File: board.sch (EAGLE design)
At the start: 27 parts

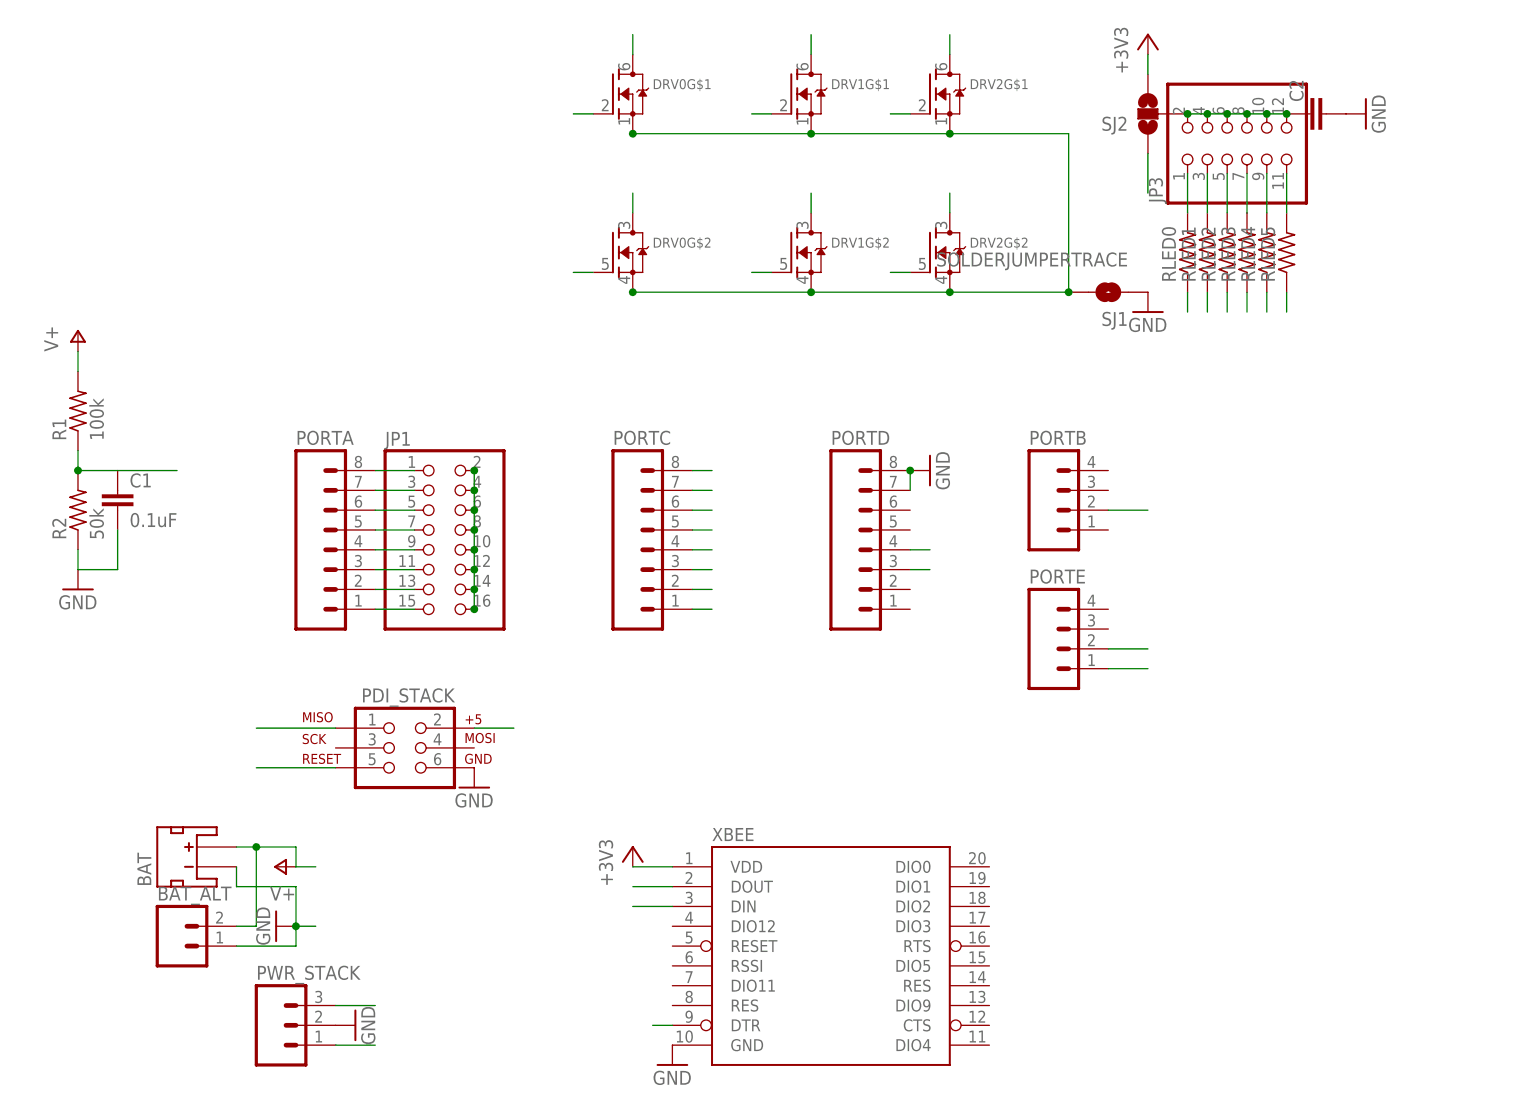
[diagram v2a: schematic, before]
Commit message: bigger cap for the leds
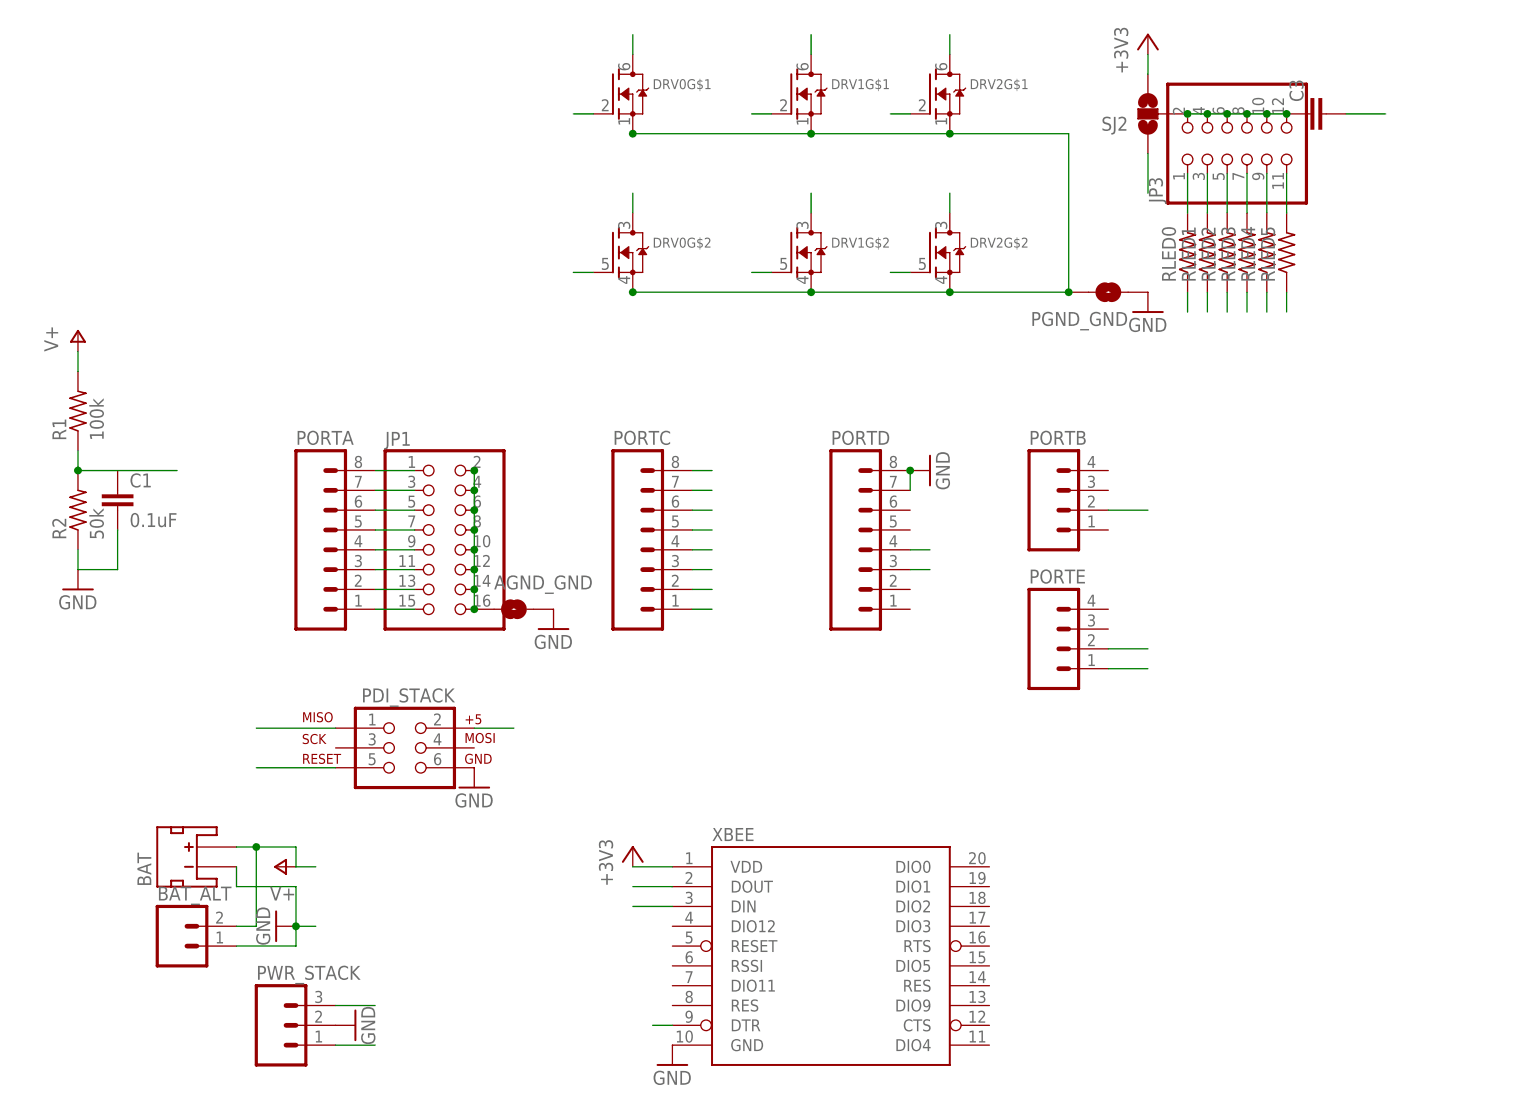
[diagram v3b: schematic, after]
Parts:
- removed C2: (no value), resistor:C-EUC0805K
- added AGND_GND: SOLDERJUMPERTRACE, SparkFun-Passives:SOLDERJUMPERTRACE
- added C3: (no value), rcl:C-EUC1210
- renumbered SJ1 to PGND_GND
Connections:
- removed net GND_PWR: DRV0G$1.S, DRV0G$2.S, DRV1G$1.S, DRV1G$2.S, DRV2G$1.S, DRV2G$2.S, PGND_GND.2
- new net PGND: C3.2, DRV0G$1.S, DRV0G$2.S, DRV1G$1.S, DRV1G$2.S, DRV2G$1.S, DRV2G$2.S, PGND_GND.2
- net AGND: now also AGND_GND.1
- net GND: now also AGND_GND.2; no longer C2.2
- net VLED: now also C3.1; no longer C2.1
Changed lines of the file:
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@@
 <part name="RLED5" library="resistor" deviceset="R-US_" device="R0805"/>
 <part name="+3V2" library="supply1" deviceset="+3V3" device=""/>
-<part name="C2" library="resistor" deviceset="C-EU" device="C0805K"/>
-<part name="GND7" library="supply1" deviceset="GND" device=""/>
-<part name="SJ1" library="SparkFun-Passives" deviceset="SOLDERJUMPER" device="TRACE"/>
+<part name="PGND_GND" library="SparkFun-Passives" deviceset="SOLDERJUMPER" device="TRACE"/>
 <part name="GND8" library="supply1" deviceset="GND" device=""/>
 <part name="JP3" library="pinhead" deviceset="PINHD-2X6" device="/90"/>
+<part name="AGND_GND" library="SparkFun-Passives" deviceset="SOLDERJUMPER" device="TRACE"/>
+<part name="GND9" library="supply1" deviceset="GND" device=""/>
+<part name="C3" library="rcl" deviceset="C-EU" device="C1210"/>
 </parts>
 <sheets>
@@
 <instance part="RLED5" gate="G$1" x="127" y="134.62" rot="R90"/>
 <instance part="+3V2" gate="G$1" x="43.18" y="58.42"/>
-<instance part="C2" gate="G$1" x="129.54" y="152.4" rot="R90"/>
-<instance part="GND7" gate="1" x="137.16" y="152.4" rot="R90"/>
-<instance part="SJ1" gate="1" x="104.14" y="129.54" rot="R180"/>
+<instance part="PGND_GND" gate="1" x="104.14" y="129.54" smashed="yes" rot="R180">
+<attribute name="NAME" x="106.68" y="127" size="1.778" layer="95" rot="R180"/>
+</instance>
 <instance part="GND8" gate="1" x="109.22" y="127"/>
 <instance part="JP3" gate="A" x="119.38" y="147.32" rot="R90"/>
+<instance part="AGND_GND" gate="1" x="27.94" y="88.9" smashed="yes">
+<attribute name="NAME" x="25.4" y="91.44" size="1.778" layer="95"/>
+</instance>
+<instance part="GND9" gate="1" x="33.02" y="86.36"/>
+<instance part="C3" gate="G$1" x="129.54" y="152.4" rot="R90"/>
 </instances>
 <busses>
@@
 </segment>
 <segment>
-<pinref part="C2" gate="G$1" pin="2"/>
-<pinref part="GND7" gate="1" pin="GND"/>
-</segment>
-<segment>
-<pinref part="SJ1" gate="1" pin="1"/>
+<pinref part="PGND_GND" gate="1" pin="1"/>
 <pinref part="GND8" gate="1" pin="GND"/>
+</segment>
+<segment>
+<pinref part="AGND_GND" gate="1" pin="2"/>
+<pinref part="GND9" gate="1" pin="GND"/>
 </segment>
 </net>
@@
 </segment>
 </net>
-<net name="GND_PWR" class="1">
+<net name="PGND" class="1">
 <segment>
 <pinref part="DRV0" gate="G$1" pin="S"/>
@@
 <junction x="43.18" y="149.86"/>
 <junction x="43.18" y="129.54"/>
-<pinref part="SJ1" gate="1" pin="2"/>
+<pinref part="PGND_GND" gate="1" pin="2"/>
 <junction x="99.06" y="129.54"/>
+</segment>
+<segment>
+<wire x1="134.62" y1="152.4" x2="139.7" y2="152.4" width="0.1524" layer="91"/>
+<pinref part="C3" gate="G$1" pin="2"/>
 </segment>
 </net>
@@
 <junction x="22.86" y="91.44"/>
 <junction x="22.86" y="88.9"/>
+<pinref part="AGND_GND" gate="1" pin="1"/>
 </segment>
 </net>
@@
 <wire x1="127" y1="152.4" x2="124.46" y2="152.4" width="0.1524" layer="91"/>
 <pinref part="SJ2" gate="G$1" pin="2"/>
-<pinref part="C2" gate="G$1" pin="1"/>
 <pinref part="JP3" gate="A" pin="2"/>
 <junction x="114.3" y="152.4"/>
@@
 <junction x="124.46" y="152.4"/>
 <pinref part="JP3" gate="A" pin="12"/>
+<pinref part="C3" gate="G$1" pin="1"/>
 <junction x="127" y="152.4"/>
 </segment>

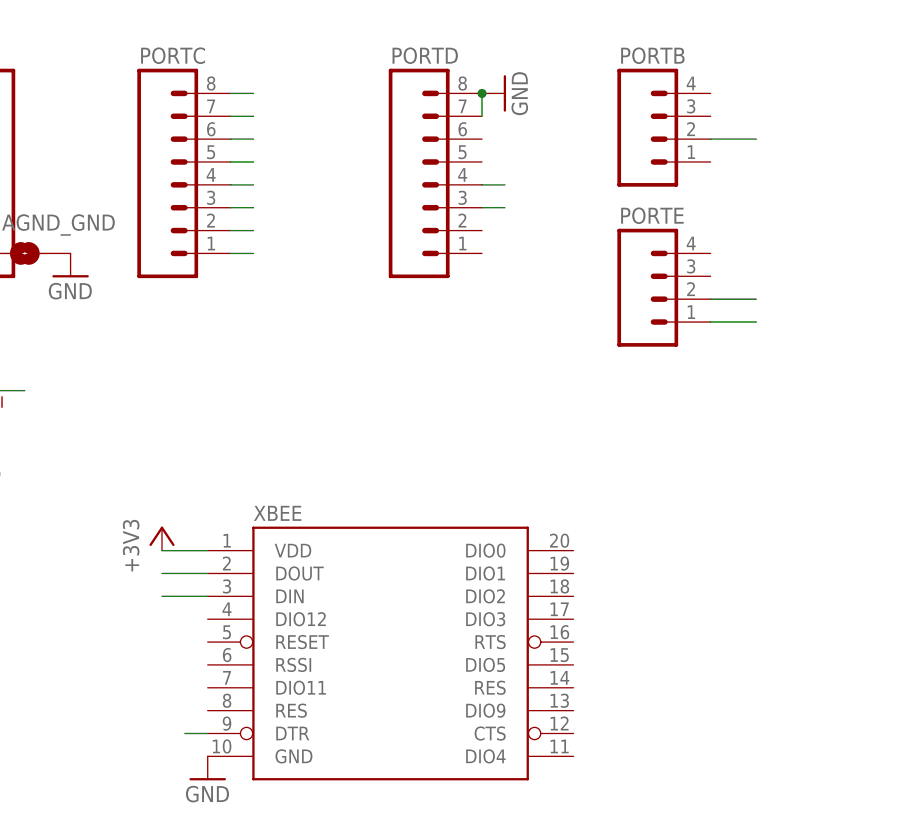
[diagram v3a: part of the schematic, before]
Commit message: xbee and xmega share aref
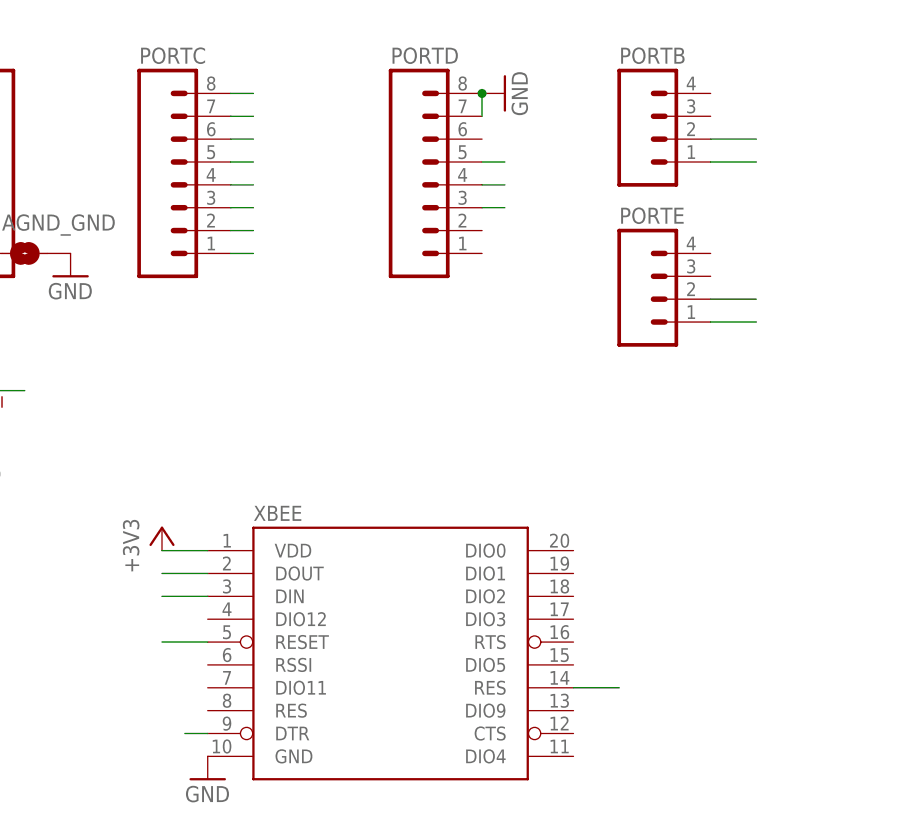
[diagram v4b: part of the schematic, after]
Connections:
- new net PB0/XMEGA_AREF: PORTB.1, XBEE.RES@14
- new net XBEE_RESET: PORTD.5, XBEE.RESET
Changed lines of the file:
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@@
+</segment>
+</net>
+<net name="PB0/XMEGA_AREF" class="0">
+<segment>
+<pinref part="PORTB" gate="G$1" pin="1"/>
+<wire x1="104.14" y1="99.06" x2="109.22" y2="99.06" width="0.1524" layer="91"/>
+</segment>
+<segment>
+<pinref part="XBEE" gate="G$1" pin="RES@14"/>
+<wire x1="88.9" y1="40.64" x2="93.98" y2="40.64" width="0.1524" layer="91"/>
+</segment>
+</net>
+<net name="XBEE_RESET" class="0">
+<segment>
+<pinref part="XBEE" gate="G$1" pin="RESET"/>
+<wire x1="48.26" y1="45.72" x2="43.18" y2="45.72" width="0.1524" layer="91"/>
+</segment>
+<segment>
+<pinref part="PORTD" gate="G$1" pin="5"/>
+<wire x1="78.74" y1="99.06" x2="81.28" y2="99.06" width="0.1524" layer="91"/>
 </segment>
 </net>
